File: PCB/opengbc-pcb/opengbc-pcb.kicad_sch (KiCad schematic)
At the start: 0 parts

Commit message: update schematics and journal and add library files
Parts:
- added C10, C29, C33, C41, C45: .01uF, symbol Device:C_Small
- added C47: 150pF, symbol Device:C_Small
- added CL1: SolderJumper_2_Bridged, symbol Jumper:SolderJumper_2_Bridged
- added P1: CART_CONN, symbol gbc_cartridge:CART_CONN
- added R27: 100R, symbol Device:R_US
- added SW1: UP, symbol Switch:SW_Push
- added SW2: DOWN, symbol Switch:SW_Push
- added SW3: RIGHT, symbol Switch:SW_Push
- added SW4: LEFT, symbol Switch:SW_Push
- added SW5: SELECT, symbol Switch:SW_Push
- added SW6: START, symbol Switch:SW_Push
- added SW7: B, symbol Switch:SW_Push
- added SW8: A, symbol Switch:SW_Push
- added U1: GameBoy_CPU_CGB_KF2007, symbol GameBoy_CPU_CGB_KF2007:GameBoy_CPU_CGB_KF2007
- added U2: AS6C62256-55STIN, SOP55P1340X120-28N, symbol AS6C62256-55STIN:AS6C62256-55STIN
- added Y1: SG-8018CE 8.388608M-TJHPA0, Oscillator:Oscillator_SMD_SeikoEpson_SG8002CE-4Pin_3.2x2.5mm, symbol Oscillator:SG-8002CE
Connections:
- new net: SW4.2, U1.4 (P01)
- new net: SW6.1, U1.127 (P13)
- new net: U1.52 (CK1), Y1.3 (OUT)
- new net: SW5.1, U1.128 (P12)
- new net: SW2.1, U1.2 (P03)
- new net: SW8.1, U1.125 (P10)
- new net: P1.10 (A4), U1.13 (A4)
- new net: P1.11 (A5), U1.14 (A5)
- new net: P1.12 (A6), U1.15 (A6)
- new net: P1.13 (A7), U1.16 (A7)
- new net: P1.14 (A8), U1.17 (A8)
- new net: P1.15 (A9), U1.18 (A9)
- new net: P1.16 (A10), U1.21 (A10)
- new net: P1.17 (A11), U1.22 (A11)
- new net: P1.18 (A12), U1.23 (A12)
- new net: P1.19 (A13), U1.24 (A13)
- new net: P1.2 (PHI), U1.5 (PHI)
- new net: P1.20 (A14), U1.25 (A14)
- new net: P1.21 (A15), U1.26 (A15)
- new net: P1.22 (D0), U1.27 (D0)
- new net: P1.23 (D1), U1.28 (D1)
- new net: P1.24 (D2), U1.29 (D2)
- new net: P1.25 (D3), U1.30 (D3)
- new net: P1.26 (D4), U1.31 (D4)
- new net: P1.27 (D5), U1.32 (D5)
- new net: P1.28 (D6), U1.33 (D6)
- new net: P1.29 (D7), U1.34 (D7)
- new net: P1.3 (~{WR}), R27.1
- new net: C47.1, P1.30 (~{RES}), U1.35 (~{RES})
- new net: P1.31 (VIN), U1.36 (VIN)
- new net: P1.4 (~{RD}), U1.7 (~{RD})
- new net: P1.5 (~{CS}), U1.8 (~{CS})
- new net: P1.6 (A0), U1.9 (A0)
- new net: P1.7 (A1), U1.10 (A1)
- new net: P1.8 (A2), U1.11 (A2)
- new net: P1.9 (A3), U1.12 (A3)
- new net: SW7.1, U1.126 (P11)
- new net: SW1.1, U1.3 (P02)
- new net: SW3.1, U1.1 (P00)
- new net: R27.2, U1.6 (~{WR})
- new net: CL1.1 (A), U1.57 (~{\NMI})
- new net: C29.1, U1.85 (VDD3)
- new net +3.3V: C33.1, CL1.2 (B), U1.107 (VDD3), U2.7 (VCC), Y1.1 (OE), Y1.4 (Vcc)
- new net +5V: C10.1, C41.1, C45.1, P1.1 (Vdd), U1.20 (VDD5), U1.43 (VDD5)
- new net DISP_FFC/B0: U1.86 (LDB0)
- new net DISP_FFC/B1: U1.87 (LDB1)
- new net DISP_FFC/B2: U1.88 (LDB2)
- new net DISP_FFC/B3: U1.89 (LDB3)
- new net DISP_FFC/B4: U1.90 (LDB4)
- new net DISP_FFC/B5: U1.91 (LDB5)
- new net DISP_FFC/CLS: U1.70 (CLS)
- new net DISP_FFC/DCLK: U1.94 (DCK)
- new net DISP_FFC/G0: U1.78 (LDG0)
- new net DISP_FFC/G1: U1.79 (LDG1)
- new net DISP_FFC/G2: U1.80 (LDG2)
- new net DISP_FFC/G3: U1.81 (LDG3)
- new net DISP_FFC/G4: U1.82 (LDG4)
- new net DISP_FFC/G5: U1.83 (LDG5)
- new net DISP_FFC/LP: U1.93 (LP)
- new net DISP_FFC/MOD: U1.68 (MOD)
- new net DISP_FFC/PS: U1.92 (PS)
- new net DISP_FFC/R0: U1.72 (LDR0)
- new net DISP_FFC/R1: U1.73 (LDR1)
- new net DISP_FFC/R2: U1.74 (LDR2)
- new net DISP_FFC/R3: U1.75 (LDR3)
- new net DISP_FFC/R4: U1.76 (LDR4)
- new net DISP_FFC/R5: U1.77 (LDR5)
- new net DISP_FFC/SPL: U1.71 (SPL)
- new net DISP_FFC/SPS: U1.69 (SPS)
- new net GND: C10.2, C29.2, C33.2, C41.2, C45.2, C47.2, P1.32 (GND), SW1.2, SW2.2, SW3.2, SW4.1, SW5.2, SW6.2, SW7.2, SW8.2, U1.108 (GND), U1.19 (GND), U1.44 (GND), U1.49 (TEST0), U1.50 (TEST1), U1.51 (TEST2), U1.54 (PSMO0), U1.55 (PSMO1), U1.58 (~{MCS0}), U1.59 (~{MCS1}), U1.84 (GND), U2.21 (VSS), Y1.2 (GND)
- new net RAM_BUS.MA0: U1.99 (MA0), U2.17 (A0)
- new net RAM_BUS.MA1: U1.98 (MA1), U2.16 (A1)
- new net RAM_BUS.MA10: U1.111 (MA10), U2.28 (A10)
- new net RAM_BUS.MA11: U1.113 (MA11), U2.2 (A11)
- new net RAM_BUS.MA12: U1.119 (MA12), U2.9 (A12)
- new net RAM_BUS.MA2: U1.97 (MA2), U2.15 (A2)
- new net RAM_BUS.MA3: U1.124 (MA3), U2.14 (A3)
- new net RAM_BUS.MA4: U1.123 (MA4), U2.13 (A4)
- new net RAM_BUS.MA5: U1.122 (MA5), U2.12 (A5)
- new net RAM_BUS.MA6: U1.121 (MA6), U2.11 (A6)
- new net RAM_BUS.MA7: U1.120 (MA7), U2.10 (A7)
- new net RAM_BUS.MA8: U1.115 (MA8), U2.4 (A8)
- new net RAM_BUS.MA9: U1.114 (MA9), U2.3 (A9)
- new net RAM_BUS.MD0: U1.100 (MD0), U2.18 (DQ0)
- new net RAM_BUS.MD1: U1.101 (MD1), U2.19 (DQ1)
- new net RAM_BUS.MD2: U1.102 (MD2), U2.20 (DQ2)
- new net RAM_BUS.MD3: U1.103 (MD3), U2.22 (DQ3)
- new net RAM_BUS.MD4: U1.104 (MD4), U2.23 (DQ4)
- new net RAM_BUS.MD5: U1.105 (MD5), U2.24 (DQ5)
- new net RAM_BUS.MD6: U1.106 (MD6), U2.25 (DQ6)
- new net RAM_BUS.MD7: U1.109 (MD7), U2.26 (DQ7)
- new net RAM_BUS.RA0: U1.116 (RA0), U2.5 (A13)
- new net RAM_BUS.RA1: U1.118 (RA1), U2.8 (A14)
- new net RAM_BUS./CS1: U1.110 (~{CS1}), U2.27 (CE#)
- new net RAM_BUS./MRD: U1.112 (~{MRD}), U2.1 (OE#)
- new net RAM_BUS./MWR: U1.117 (~{MWR}), U2.6 (WE#)
- no-connect marks 0 -> 11
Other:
- added sheet Audio (audio.kicad_sch)
- added sheet DISP_FFC (disp_ffc.kicad_sch)
- added sheet EXT_CONN (ext_conn.kicad_sch)
- added sheet IR_PORT (ir.kicad_sch)

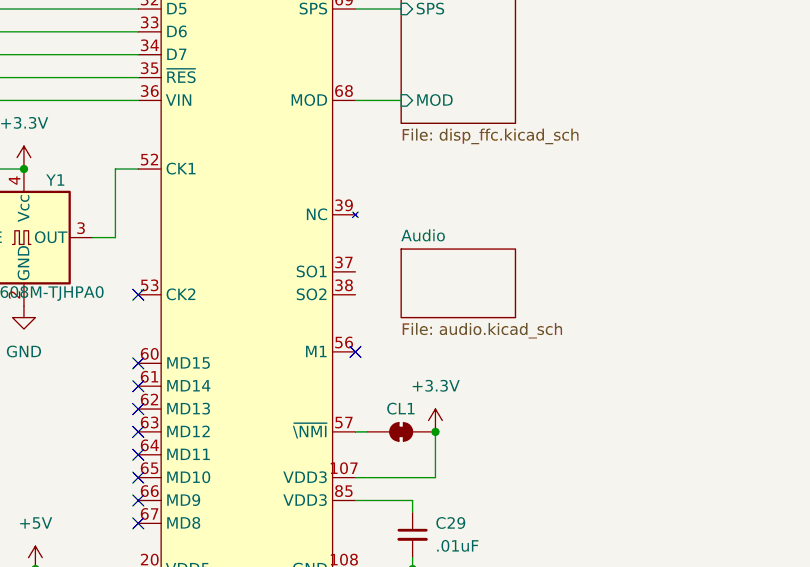
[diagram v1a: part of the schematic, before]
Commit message: update audio schematic
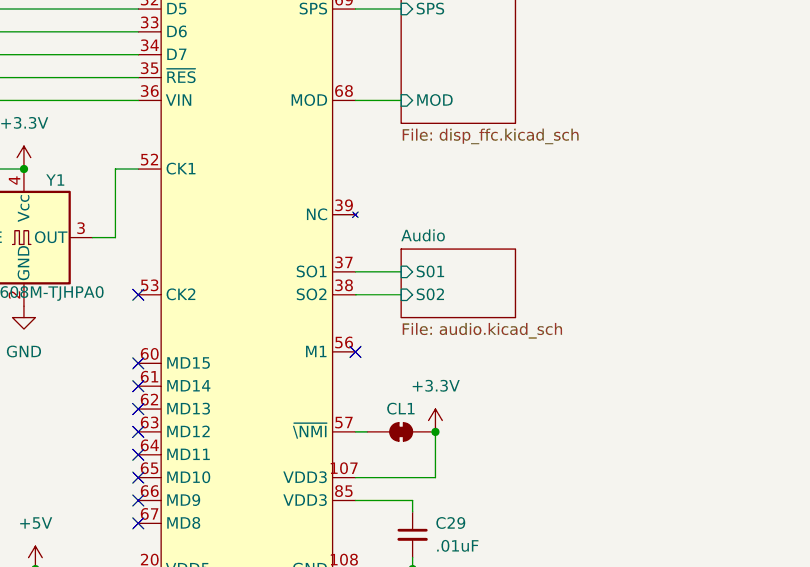
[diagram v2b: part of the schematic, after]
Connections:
- net Audio/S01: now reaches U1.37 (SO1)
- net Audio/S02: now reaches U1.38 (SO2)
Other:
- sheet Audio ports: added S01, S02; removed none
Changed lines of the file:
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@@
 	(wire
 		(pts
+			(xy 87.63 137.16) (xy 92.71 137.16)
+		)
+		(stroke
+			(width 0)
+			(type default)
+		)
+	)
+	(wire
+		(pts
 			(xy 41.91 123.19) (xy 50.8 123.19)
 		)
@@
 	(wire
 		(pts
+			(xy 87.63 134.62) (xy 92.71 134.62)
+		)
+		(stroke
+			(width 0)
+			(type default)
+		)
+	)
+	(wire
+		(pts
 			(xy 87.63 44.45) (xy 92.71 44.45)
 		)
@@
 			)
 		)
+		(pin "S01" input
+			(at 92.71 134.62 180)
+			(effects
+				(font
+					(size 1.27 1.27)
+				)
+				(justify left)
+			)
+		)
+		(pin "S02" input
+			(at 92.71 137.16 180)
+			(effects
+				(font
+					(size 1.27 1.27)
+				)
+				(justify left)
+			)
+		)

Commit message: whole bunch of schematic updates
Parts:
- added C11: .033uF, symbol Device:C_Small
- added C9: 1uF, symbol Device:C_Small
- added U4: TPS3840DL35, SOT95P280X145-5N, symbol TPS3840DL35DBVR:TPS3840DL35DBVR
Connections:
- net +3.3V: now also C10.1, C29.1, P1.1 (Vdd), U1.85 (VDD3)
- net +5V: now also C9.1, U4.2 (VDD); no longer C10.1, P1.1 (Vdd)
- net GND: now also C11.2, C9.2, U4.3 (GND)
- net at C47.1, P1.30 (~{RES}), U1.35 (~{RES}): now also U4.1 (~{RESET})
- net EXT_CONN/SCK: now reaches U1.40 (SCK)
- net EXT_CONN/SIN: now reaches U1.41 (SIN)
- net EXT_CONN/SOUT: now reaches U1.42 (SOUT)
- net IR_PORT/R0: now reaches U1.45 (R0)
- net IR_PORT/R1: now reaches U1.46 (R1)
- net IR_PORT/R2: now reaches U1.47 (R2)
- net IR_PORT/R3: now reaches U1.48 (R3)
- net EXT_CONN/R4: now reaches U1.96 (R4)
- new net: C11.1, U4.5 (CT)
- no-connect marks 11 -> 12
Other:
- added sheet Power (pwr.kicad_sch)
- sheet EXT_CONN ports: added R4, SCK, SIN, SOUT; removed none
- sheet IR_PORT ports: added R0, R1, R2, R3; removed none
- moved on the sheet: C10, C29, C33, C41, C45, C47, CL1, P1, R27, U1B, Y1

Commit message: :eyes:
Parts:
- removed SW1: UP, symbol Switch:SW_Push
- removed SW2: DOWN, symbol Switch:SW_Push
- removed SW3: RIGHT, symbol Switch:SW_Push
- removed SW4: LEFT, symbol Switch:SW_Push
- removed SW5: SELECT, symbol Switch:SW_Push
- removed SW6: START, symbol Switch:SW_Push
- removed SW7: B, symbol Switch:SW_Push
- removed SW8: A, symbol Switch:SW_Push
- added U8: gbc_buttons, gbc_repro_lib:gbc_buttons, symbol gbc_buttons:gbc_buttons
- C10, C29, C33, C41, C45: footprint (none) -> Capacitor_SMD:C_0603_1608Metric_Pad1.08x0.95mm_HandSolder; Mouser Part Number (none) -> 81-GRT188R72A103KE1D
- C11: footprint (none) -> Capacitor_SMD:C_0603_1608Metric_Pad1.08x0.95mm_HandSolder; Mouser Part Number (none) -> 603-CC603JRX7R8BB333
- C47: footprint (none) -> Capacitor_SMD:C_0603_1608Metric_Pad1.08x0.95mm_HandSolder; Mouser Part Number (none) -> 187-CL10C151JB81PNC
- C9: footprint (none) -> Capacitor_SMD:C_0603_1608Metric_Pad1.08x0.95mm_HandSolder; Mouser Part Number (none) -> 963-JMK107BJ105MA-T
- CL1: footprint (none) -> Jumper:SolderJumper-2_P1.3mm_Bridged_RoundedPad1.0x1.5mm
- P1: footprint (none) -> gbc_repro_lib:gbc_mgb_cart_slot; now left out of the parts list
- R27: footprint (none) -> Resistor_SMD:R_0603_1608Metric_Pad0.98x0.95mm_HandSolder; Mouser Part Number (none) -> 791-RMC1/16-101JTP10
- U1: footprint (none) -> Package_QFP:LQFP-128_14x20mm_P0.5mm; now left out of the parts list
- U2: footprint SOP55P1340X120-28N -> gbc_repro_lib:TSOP-I-28_11.8x8mm_P0.55mm
- U4: footprint SOT95P280X145-5N -> Package_TO_SOT_SMD:SOT-23-5_HandSoldering
- Y1: Mouser Part Number (none) -> 732-CE838868MTJHPA
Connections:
- net +3.3V: no longer C10.1, P1.1 (Vdd)
- net +5V: now also C10.1, P1.1 (Vdd)
- net GND: now also U8.10 (GND)
- net at U1.4 (P01): now also U8.4 (Left)
- net at U1.127 (P13): now also U8.7 (Start)
- net at U1.128 (P12): now also U8.8 (Select)
- net at U1.2 (P03): now also U8.3 (Down)
- net at U1.125 (P10): now also U8.6 (A)
- net at U1.126 (P11): now also U8.5 (B)
- net at U1.3 (P02): now also U8.1 (Up)
- net at U1.1 (P00): now also U8.2 (Right)
- new net Power/B+: U8.9 (Batt+)
- new net Power/B-: U8.11 (Batt-)
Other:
- sheet Power ports: added B+, B-; removed none

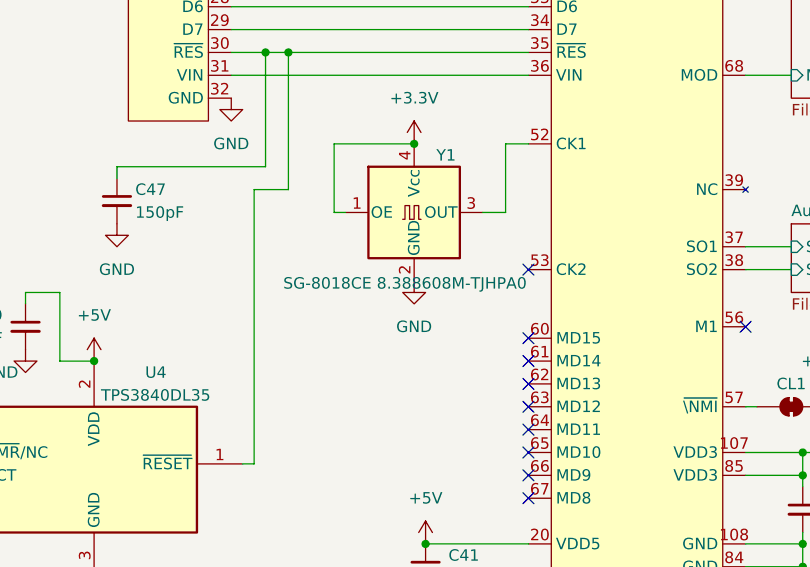
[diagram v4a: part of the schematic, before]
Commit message: update schematic
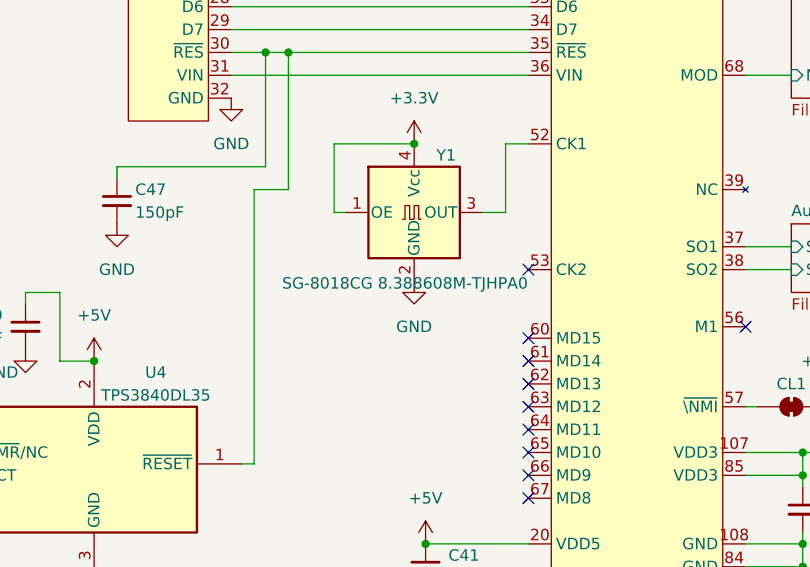
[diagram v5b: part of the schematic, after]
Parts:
- Y1: value SG-8018CE 8.388608M-TJHPA0 -> SG-8018CG 8.388608M-TJHPA0
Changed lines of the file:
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@@
 			)
 		)
-		(property "Value" "SG-8018CE 8.388608M-TJHPA0"
+		(property "Value" "SG-8018CG 8.388608M-TJHPA0"
 			(at 75.184 138.684 0)
 			(effects

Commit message: I HATE KICAD
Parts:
- U1: footprint Package_QFP:LQFP-128_14x20mm_P0.5mm -> gbc_repro_lib:LQFP-128_14x20mm_P0.5mm
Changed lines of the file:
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@@
 			)
 		)
-		(property "Footprint" "Package_QFP:LQFP-128_14x20mm_P0.5mm"
+		(property "Footprint" "gbc_repro_lib:LQFP-128_14x20mm_P0.5mm"
 			(at 181.61 67.31 0)
 			(effects
@@
 			)
 		)
-		(property "Footprint" "Package_QFP:LQFP-128_14x20mm_P0.5mm"
+		(property "Footprint" "gbc_repro_lib:LQFP-128_14x20mm_P0.5mm"
 			(at 101.6 34.29 0)
 			(effects
